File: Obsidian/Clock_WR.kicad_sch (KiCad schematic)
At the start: 85 parts, among them U12 LP5951MF-3.0/NOPB, U13 LM336M-2.5, U14 DAC8551IADGKR, U15 DAC8551IADGKR, U16 CDCM61002RHBR, U3 Si5351A-B-GT, U30 NC7SZ04M5X, Y1 25MHz, Y2 SIT5001AC-GE-33VQ-25.000000X, Y3 OSC_20MHZ_IQD_LFVCXO026156, Y6 ABM8W-25.0000MHZ-8-D1X-T3

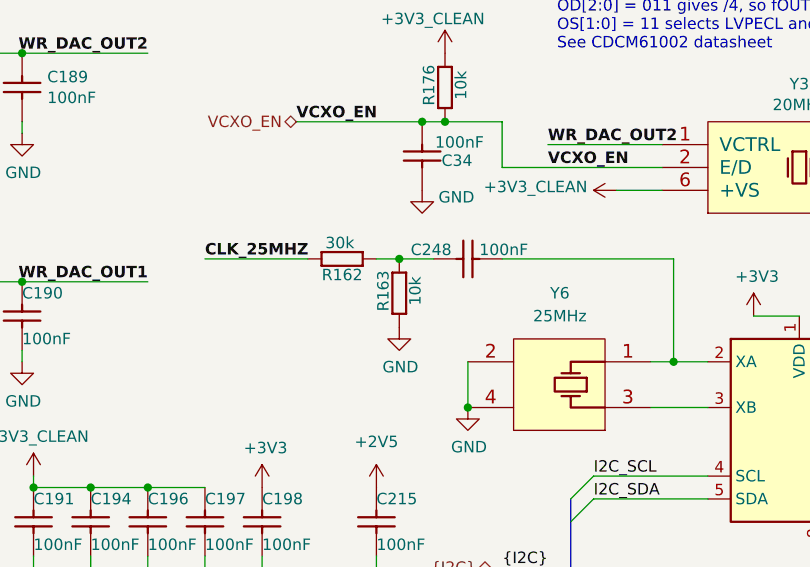
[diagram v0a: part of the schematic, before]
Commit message: putting input resistor/capacitor of U3 in DNP (see #29)
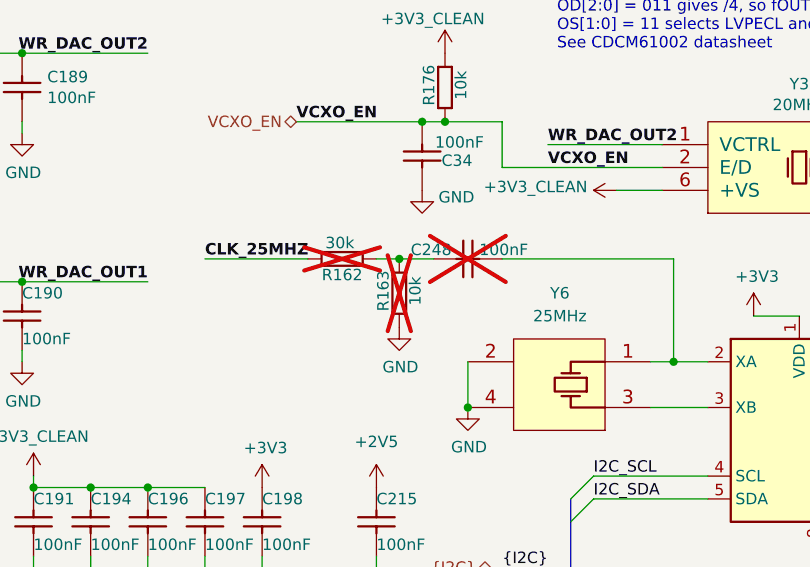
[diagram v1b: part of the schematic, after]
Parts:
- C248, R162, R163: now not fitted; now left out of the parts list
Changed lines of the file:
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@@
 		(unit 1)
 		(exclude_from_sim no)
-		(in_bom yes)
+		(in_bom no)
 		(on_board yes)
-		(dnp no)
+		(dnp yes)
 		(property "Reference" "R162"
 			(at 148.59 126.238 0)
@@
 		(unit 1)
 		(exclude_from_sim no)
-		(in_bom yes)
+		(in_bom no)
 		(on_board yes)
-		(dnp no)
+		(dnp yes)
 		(property "Reference" "C248"
 			(at 156.21 123.444 0)
@@
 		(unit 1)
 		(exclude_from_sim no)
-		(in_bom yes)
+		(in_bom no)
 		(on_board yes)
-		(dnp no)
+		(dnp yes)
 		(property "Reference" "R163"
 			(at 153.162 128.016 0)

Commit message: Update schematic for out of stock components
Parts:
- C201, C203: footprint Footprint:CAPC1709X100N -> Capacitor_SMD:C_1206_3216Metric; LCSC C138601 -> C527365
- R176: LCSC C60490 -> C2077241
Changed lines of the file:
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@@
 			)
 		)
-		(property "Footprint" "Footprint:CAPC1709X100N"
+		(property "Footprint" "Capacitor_SMD:C_1206_3216Metric"
 			(at 145.542 66.04 0)
 			(effects
@@
 			)
 		)
-		(property "Datasheet" "${KIPRJMOD}/datasheet/C138601.pdf"
+		(property "Datasheet" "${KIPRJMOD}/datasheet/C527365.pdf"
 			(at 161.544 66.04 0)
 			(effects
@@
 			)
 		)
-		(property "LCSC" "C138601"
+		(property "LCSC" "C527365"
 			(at 172.72 66.04 90)
 			(effects
@@
 			)
 		)
-		(property "Datasheet" "${KIPRJMOD}/datasheet/C60490.pdf"
+		(property "Datasheet" "${KIPRJMOD}/datasheet/C2077241.pdf"
 			(at 168.783 109.22 0)
 			(effects
@@
 			)
 		)
-		(property "LCSC" "C60490"
+		(property "LCSC" "C2077241"
 			(at 160.02 109.22 0)
 			(effects
@@
 			)
 		)
-		(property "Footprint" "Footprint:CAPC1709X100N"
+		(property "Footprint" "Capacitor_SMD:C_1206_3216Metric"
 			(at 151.892 66.04 0)
 			(effects
@@
 			)
 		)
-		(property "Datasheet" "${KIPRJMOD}/datasheet/C138601.pdf"
+		(property "Datasheet" "${KIPRJMOD}/datasheet/C527365.pdf"
 			(at 167.894 66.04 0)
 			(effects
@@
 			)
 		)
-		(property "LCSC" "C138601"
+		(property "LCSC" "C527365"
 			(at 179.07 66.04 90)
 			(effects

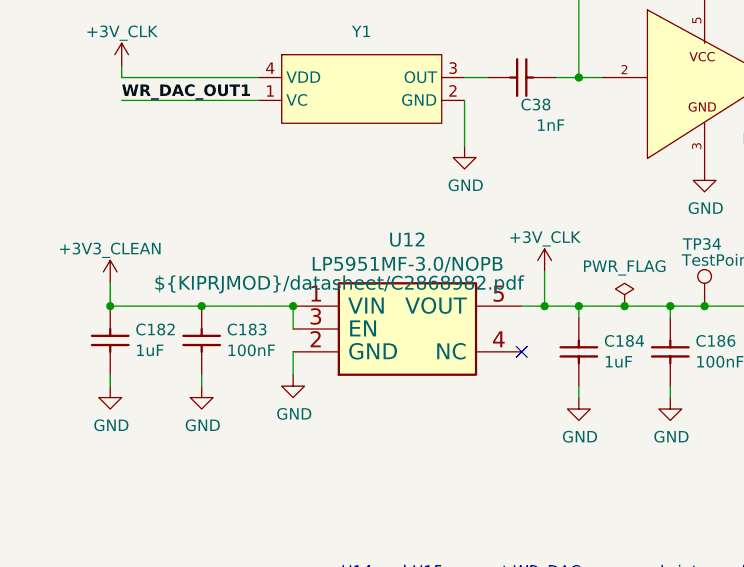
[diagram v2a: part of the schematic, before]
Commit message: Correct offset and position on JLCPCB, re-generate production folder
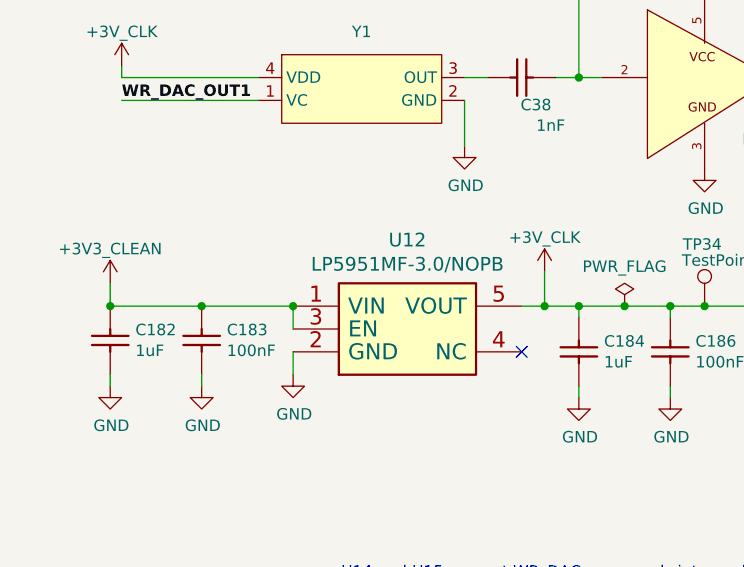
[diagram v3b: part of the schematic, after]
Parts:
- C201, C203: value CC0603_10UF_6.3V_20%_Y5V -> CC0805_10UF_6.3V_20%_Y5V; footprint Capacitor_SMD:C_1206_3216Metric -> Capacitor_SMD:C_0805_2012Metric; LCSC C527365 -> C88484
- U16: FT Rotation Offset 0 -> 270
- U30: FT Rotation Offset (none) -> 180
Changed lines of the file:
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@@
 			)
 		)
-		(property "FT Rotation Offset" "0"
+		(property "FT Rotation Offset" "270"
 			(at 196.85 22.86 0)
 			(effects
@@
 					(size 1.524 1.524)
 				)
+				(hide yes)
 			)
 		)
@@
 			)
 		)
-		(property "Value" "CC0603_10UF_6.3V_20%_Y5V"
+		(property "Value" "CC0805_10UF_6.3V_20%_Y5V"
 			(at 166.116 66.04 0)
 			(effects
@@
 			)
 		)
-		(property "Footprint" "Capacitor_SMD:C_1206_3216Metric"
+		(property "Footprint" "Capacitor_SMD:C_0805_2012Metric"
 			(at 145.542 66.04 0)
 			(effects
@@
 			)
 		)
-		(property "LCSC" "C527365"
+		(property "LCSC" "C88484"
 			(at 172.72 66.04 90)
 			(effects
@@
 			)
 		)
-		(property "Value" "CC0603_10UF_6.3V_20%_Y5V"
+		(property "Value" "CC0805_10UF_6.3V_20%_Y5V"
 			(at 172.466 66.04 0)
 			(effects
@@
 			)
 		)
-		(property "Footprint" "Capacitor_SMD:C_1206_3216Metric"
+		(property "Footprint" "Capacitor_SMD:C_0805_2012Metric"
 			(at 151.892 66.04 0)
 			(effects
@@
 			)
 		)
-		(property "LCSC" "C527365"
+		(property "LCSC" "C88484"
 			(at 179.07 66.04 90)
 			(effects
@@
 			(at 86.36 16.51 0)
 			(effects
+				(font
+					(size 1.27 1.27)
+				)
+				(hide yes)
+			)
+		)
+		(property "FT Rotation Offset" "180"
+			(at 86.36 16.51 0)
+			(effects

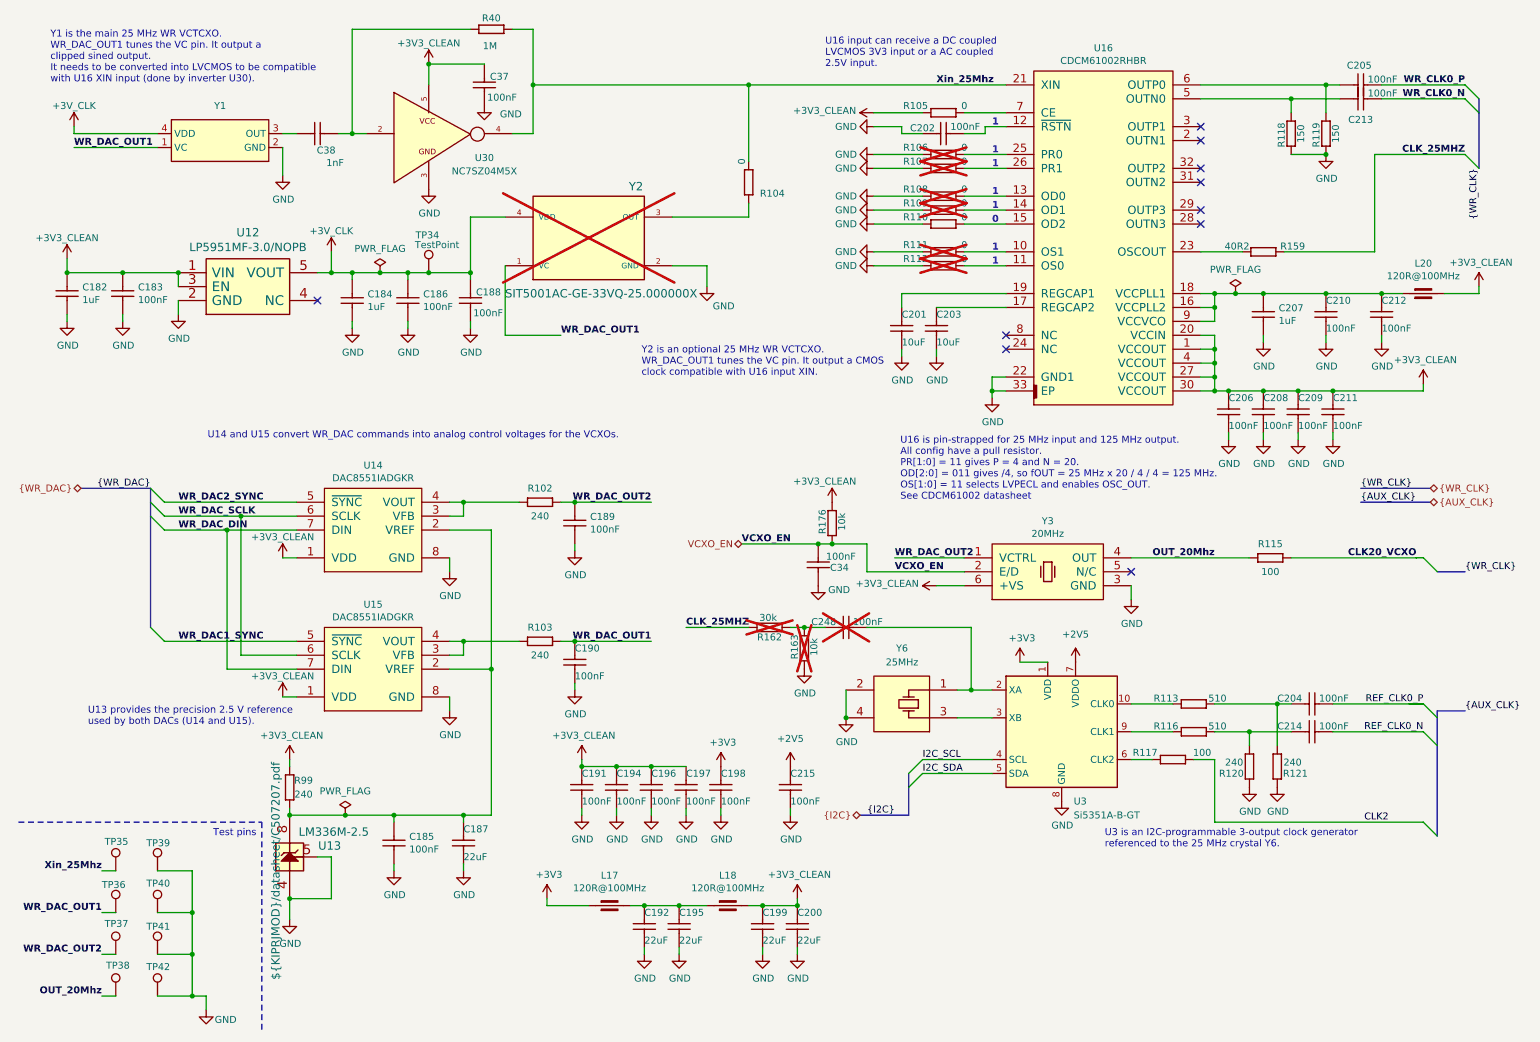
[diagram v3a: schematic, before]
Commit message: As ordered 10/06/26
Signed-off-by: Jean Alinei <jean.alinei@owntech.org>
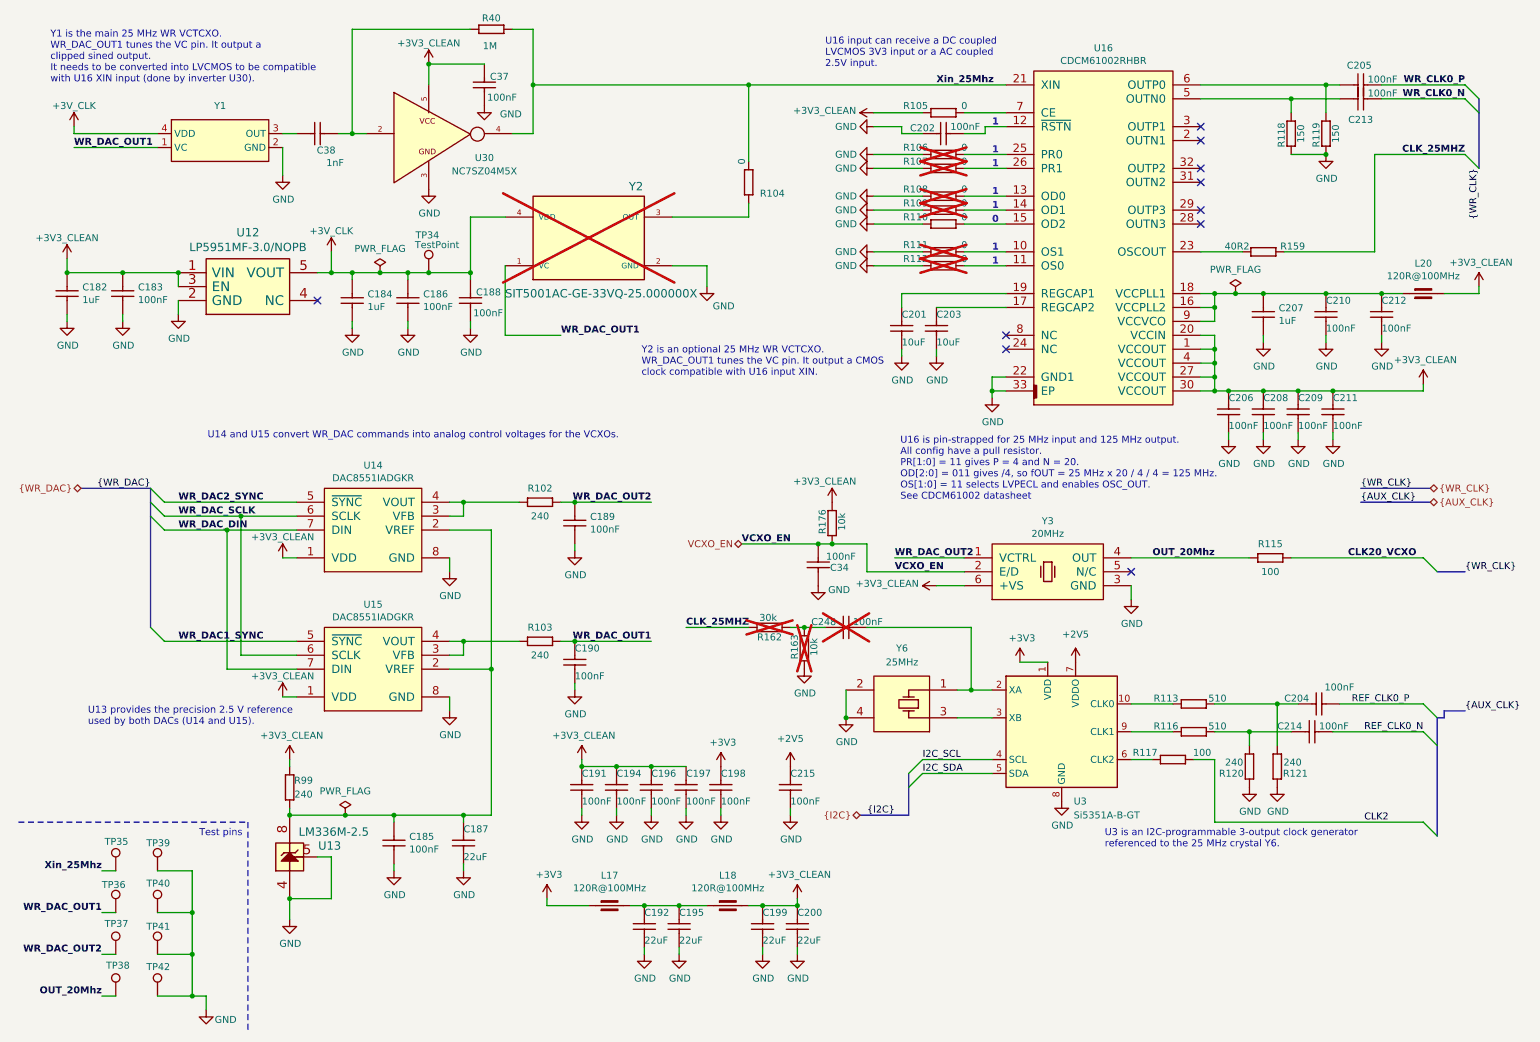
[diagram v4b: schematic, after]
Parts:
- U30: Availability (none) -> In Stock; Check_prices (none) -> https://www.snapeda.com/parts/NC7SZ04M5X/Onsemi/view-part/?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; Description_1 (none) -> The NC7SZ04 is a single inverter from Fairchild's Ultra Hig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; MF (none) -> ON Semiconductor; MP (none) -> NC7SZ04M5X; MPN (none) -> NC7SZ04M5X; OC_FARNELL (none) -> 1417667; OC_NEWARK (none) -> 58K1973; PACKAGE (none) -> SOT-23-5; Package (none) -> SOT-23 Fairchild Semiconductor; Price (none) -> None; SUPPLIER (none) -> Fairchild; SnapEDA_Link (none) -> https://www.snapeda.com/parts/NC7SZ04M5X/Onsemi/view-part/?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
- Y1: LCSC Part Name (none) -> VCTCXO 3225 4P 25MHz Clipped Sine wave 3.3V ±1ppm -40°C~+85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; Manufacturer (none) -> HCI(杭晶); Manufacturer Part (none) -> 9132S-Y25.000N33DT1J; Supplier (none) -> LCSC; Supplier Part (none) -> C52954962
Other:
- moved on the sheet: C204
